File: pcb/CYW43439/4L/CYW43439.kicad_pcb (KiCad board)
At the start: 4 copper layers, 29.9 x 30.2 mm, 36 parts, among them J1 GPIOs, J2 SPI, J3 Power, J4 RP-SMA Female, U1 CYW43439KUBGT, Y1 Crystal

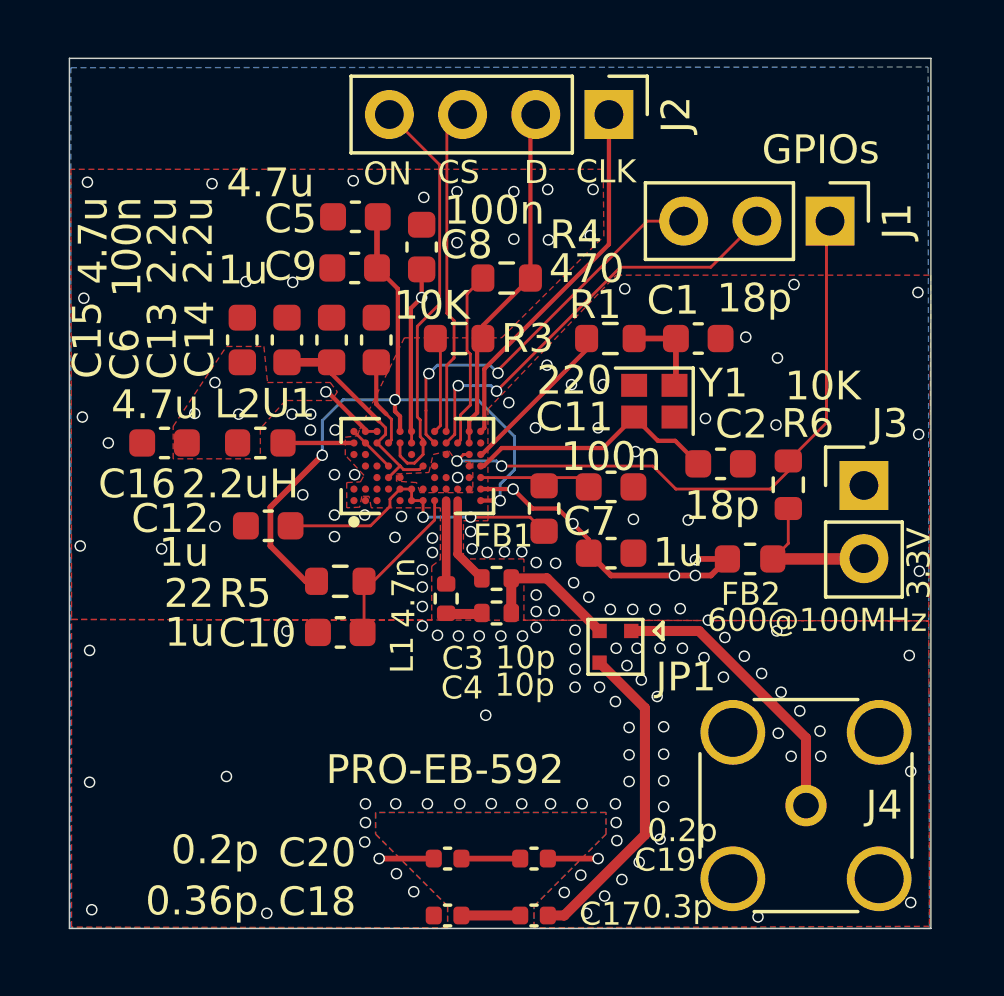
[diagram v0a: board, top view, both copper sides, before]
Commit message: [pcb] add USB-A
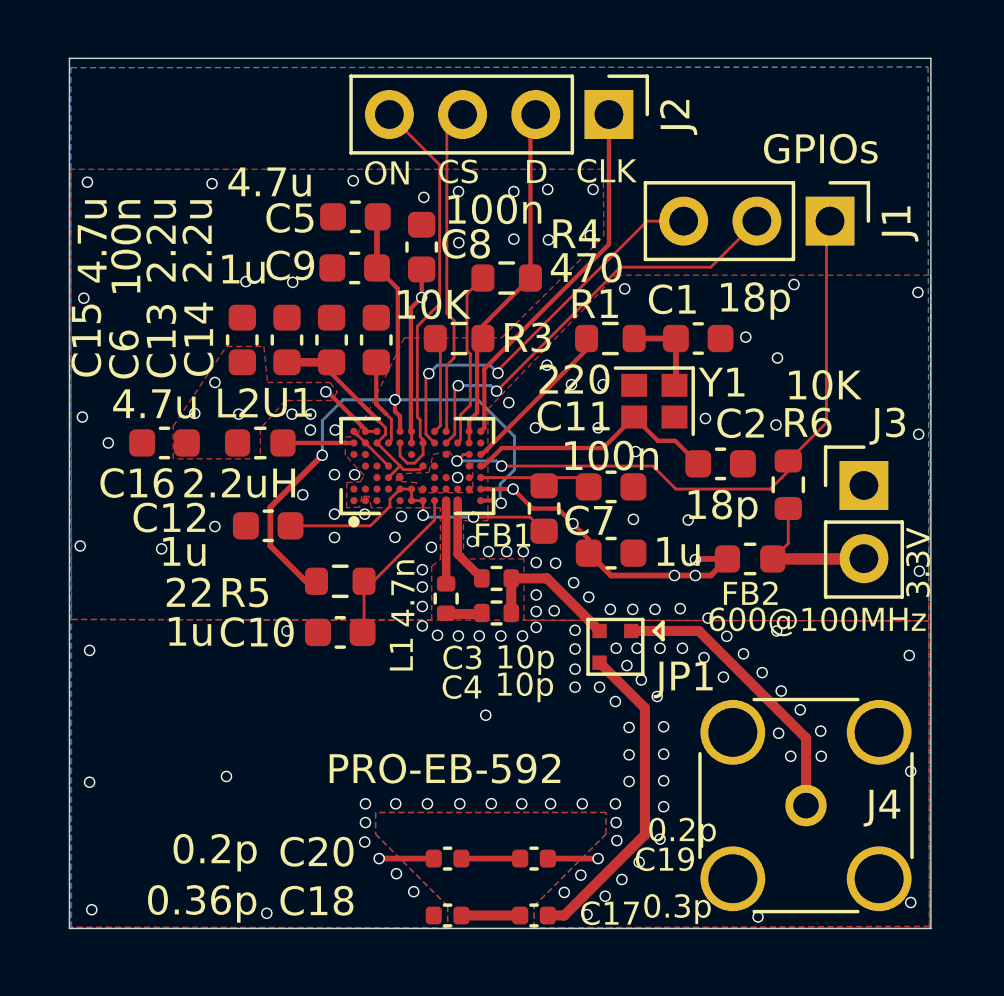
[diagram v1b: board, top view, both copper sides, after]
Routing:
- net GND: vias 147 -> 145

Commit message: [CYW43439] fix VDDBAT/LDO_IN short circuited, others
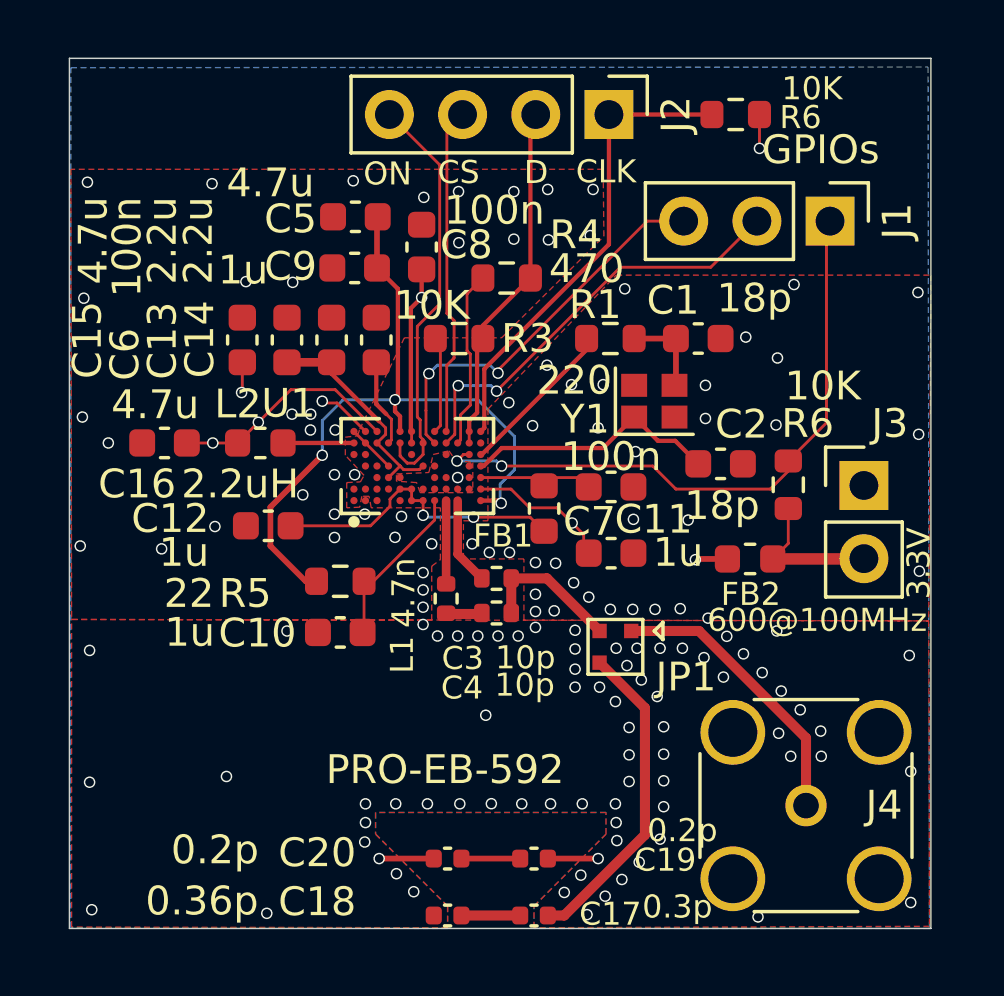
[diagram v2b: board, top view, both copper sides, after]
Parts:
- added R6: 10K, Resistor_SMD:R_0603_1608Metric, F.Cu at (148.8, 84.1)
- turned Y1 to 0 degrees
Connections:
- C16 pad 1: VDDBAT -> VIN_LDO
- C7 pad 1: VDDBAT -> VIN_LDO
- L2 pad 1: VDDBAT -> VIN_LDO
- U1 pad C7: VDDBAT -> VIN_LDO
- U1 pad M2: VDDBAT -> VIN_LDO
- Y1 pad 1: Net-(C1-Pad1) -> Net-(U1-WLRF_XTAL_XOP)
- Y1 pad 3: Net-(U1-WLRF_XTAL_XOP) -> Net-(C1-Pad1)
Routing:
- net VIN_LDO: track 0.00 -> 12.7 mm, vias 0 -> 3
- net VDDBAT: track 20.0 -> 10.3 mm, vias 10 -> 4
- net WL_CLK: track 12.8 -> 16.4 mm
- net GND: track 5.51 -> 6.69 mm, vias 145 -> 146
- added copper zone on In2.Cu, net VIN_LDO
- removed copper zone on F.Cu, net VDDBAT
